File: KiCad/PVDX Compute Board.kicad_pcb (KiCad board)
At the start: 2 copper layers, 66.5 x 64 mm, 43 parts, among them IC1 MIC5350-SGYMT-TR, J1 Conn_02x06_Counter_Clockwise, J2 USB_C_Receptacle_USB2.0_14P, J3 Conn_01x07, J4 Conn_01x06, U1 EM008LX, U2 EM008LX, U3 EM008LX, U4 SAMD51, X1 2x5 0.05" SWD

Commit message: update draft to 11/13 version
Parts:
- added C5: 0.1 uF, Capacitor_SMD:C_0201_0603Metric, F.Cu at (148.3, 54.5)
- added C6: 0.1 uF, Capacitor_SMD:C_0201_0603Metric, F.Cu at (152.8, 54.5)
- added C7: 0.1 uF, Capacitor_SMD:C_0201_0603Metric, F.Cu at (148.3, 75.0)
- added C8: 0.1 uF, Capacitor_SMD:C_0201_0603Metric, F.Cu at (154.8, 75.0)
- added J6: Conn_02x11_Counter_Clockwise, Connector_Hirose:Hirose_DF11-22DP-2DSA_2x11_P2.00mm_Vertical, F.Cu at (173.0, 93.0)
- added R14: 10K, Resistor_SMD:R_0603_1608Metric, F.Cu at (202.0, 72.5)
- added R15: 10K, Resistor_SMD:R_0603_1608Metric, F.Cu at (203.0, 65.3)
- added R16: 10K, Resistor_SMD:R_0603_1608Metric, F.Cu at (151.8, 63.0)
- added R17: 10K, Resistor_SMD:R_0603_1608Metric, F.Cu at (151.7, 74.5)
- added U5: TXS0108EPW, Package_SO:TSSOP-20_4.4x6.5mm_P0.65mm, F.Cu at (151.5, 58.5)
- added U6: TXS0108EPW, Package_SO:TSSOP-20_4.4x6.5mm_P0.65mm, F.Cu at (151.5, 70.0)
- added U7: TMUX1108PW, Package_SO:TSSOP-16_4.4x5mm_P0.65mm, F.Cu at (205.1, 92.0)
- CIN1, CIN4: value 10 μF -> 10 uF
- CIN2: value 0.1 μF -> 0.1 uF
- J3: footprint Connector_Harwin:Harwin_M20-89007xx_1x07_P2.54mm_Horizontal -> Connector_Molex:Molex_Micro-Latch_53253-0770_1x07_P2.00mm_Vertical
- J4: footprint Connector_Harwin:Harwin_M20-89006xx_1x06_P2.54mm_Horizontal -> Connector_Molex:Molex_Micro-Latch_53253-0670_1x06_P2.00mm_Vertical
- L1: value 10 μH -> 10 uH
- R11: footprint Adafruit Grand Central M4 Express rev B:0603-NO -> Resistor_SMD:R_0603_1608Metric
- moved CIN1 61.9 mm to (216.8, 58.5)
- moved CIN2 61.9 mm to (216.8, 60.3)
- moved J1 61.9 mm to (213.8, 59.1)
- moved R7 61.9 mm to (213.4, 68.8)
- moved H3 22.5 mm to (216.1, 96.6)
- moved H4 17.0 mm to (144.4, 96.5)
- moved J4 14.8 mm to (185.3, 25.2)
- moved H2 14.7 mm to (216.1, 24.9)
- moved R3 10.7 mm to (158.0, 48.0), turned to 0 degrees
- moved ON1 8.12 mm to (166.0, 33.5)
- moved R8 7.55 mm to (166.0, 29.5), turned to -90 degrees
- moved J3 7.28 mm to (152.9, 44.0), turned to 90 degrees
- moved H1 2.36 mm to (144.4, 24.9)
- moved R2 2.00 mm to (165.5, 63.0)
- moved R5 0.83 mm to (170.5, 57.0), turned to 90 degrees
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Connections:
- net 3.3V renamed 3V3
- C4 pad 1: 1.8V -> 1V8
- IC1 pad 7: 1.8V -> 1V8
- R1 pad 1: 1.8V -> 1V8
- R1 pad 2: PC14 -> PC14 1V8
- R2 pad 1: 1.8V -> 1V8
- R2 pad 2: PC15 -> PC15 1V8
- R3 pad 1: 1.8V -> 1V8
- R3 pad 2: PC12 -> PC12 1V8
- R4 pad 1: 1.8V -> PC05 1V8
- R4 pad 2: PC05 -> 1V8
- R5 pad 1: 1.8V -> PC07 1V8
- R5 pad 2: PC07 -> 1V8
- R6 pad 1: 1.8V -> PC10 1V8
- R6 pad 2: PC10 -> 1V8
- U1 pad 1: PC04 -> PC04 1V8
- U1 pad 2: PD11 (MISO) -> PD11 (MISO) 1V8
- U1 pad 3: PC14 -> PC14 1V8
- U1 pad 5: PD08 (MOSI) -> PD08 (MOSI) 1V8
- U1 pad 6: PD09 (SCK) -> PD09 (SCK) 1V8
- U1 pad 7: PC05 -> PC05 1V8
- U1 pad 8: 1.8V -> 1V8
- U2 pad 1: PC06 -> PC06 1V8
- U2 pad 2: PD11 (MISO) -> PD11 (MISO) 1V8
- U2 pad 3: PC15 -> PC15 1V8
- U2 pad 5: PD08 (MOSI) -> PD08 (MOSI) 1V8
- U2 pad 6: PD09 (SCK) -> PD09 (SCK) 1V8
- U2 pad 7: PC07 -> PC07 1V8
- U2 pad 8: 1.8V -> 1V8
- U3 pad 1: PC11 -> PC11 1V8
- U3 pad 2: PD11 (MISO) -> PD11 (MISO) 1V8
- U3 pad 3: PC12 -> PC12 1V8
- U3 pad 5: PD08 (MOSI) -> PD08 (MOSI) 1V8
- U3 pad 6: PD09 (SCK) -> PD09 (SCK) 1V8
- U3 pad 7: PC10 -> PC10 1V8
- U3 pad 8: 1.8V -> 1V8
- U4 pad 10: unconnected-(U4B-PA03/AIN01-Pad10) -> AIN01
- U4 pad 125: unconnected-(U4C-PB00/AIN12-Pad125) -> AIN12
- U4 pad 126: unconnected-(U4C-PB01/AIN13-Pad126) -> AIN13
- U4 pad 127: unconnected-(U4C-PB02/AIN14-Pad127) -> AIN14
- U4 pad 128: unconnected-(U4C-PB03/AIN15-Pad128) -> AIN15
- U4 pad 19: unconnected-(U4C-PB08/AIN02-Pad19) -> AIN02
- U4 pad 20: unconnected-(U4C-PB09/AIN03-Pad20) -> AIN03
- U4 pad 21: unconnected-(U4B-PA04/AIN04-Pad21) -> AIN04
- U4 pad 22: unconnected-(U4B-PA05/AIN05-Pad22) -> AIN05
- U4 pad 23: unconnected-(U4B-PA06/AIN06-Pad23) -> AIN06
- U4 pad 24: unconnected-(U4B-PA07/AIN07-Pad24) -> AIN07
- U4 pad 33: unconnected-(U4B-PA08/AIN08-Pad33) -> AIN08
- U4 pad 34: unconnected-(U4B-PA09/AIN09-Pad34) -> AIN09
- U4 pad 35: unconnected-(U4B-PA10/AIN10-Pad35) -> AIN10
- U4 pad 36: unconnected-(U4B-PA11/AIN11-Pad36) -> AIN11
- U4 pad 9: unconnected-(U4B-PA02/AIN00-Pad9) -> AIN00
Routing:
- net 1V8: track 0.00 -> 118.9 mm, vias 0 -> 6
- net 5V: track 48.3 -> 123.1 mm, vias 3 -> 6
- net 1.8V: track 71.7 -> 0.00 mm, vias 2 -> 0
- net GND: track 300.0 -> 370.9 mm, vias 30 -> 25
- net PD21: track 82.2 -> 15.8 mm
- net PD09 (SCK) 1V8: track 0.00 -> 56.8 mm, vias 0 -> 4
- net PC05 1V8: track 0.00 -> 56.5 mm, vias 0 -> 2
- net PD08 (MOSI) 1V8: track 0.00 -> 55.4 mm, vias 0 -> 5
- net PA16 (SCL): track 63.4 -> 17.3 mm, vias 2 -> 0
- net PD11 (MISO) 1V8: track 0.00 -> 44.6 mm, vias 0 -> 5
- net PA17 (SDA): track 62.8 -> 20.6 mm, vias 2 -> 0
- net AIN00: track 0.00 -> 40.5 mm
- net PC05: track 16.9 -> 52.5 mm, vias 2 -> 0
- net PC12 1V8: track 0.00 -> 35.1 mm, vias 0 -> 2
- net PC10 1V8: track 0.00 -> 31.2 mm, vias 0 -> 2
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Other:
- board size 66.5 x 64 mm -> 82.5 x 82.5 mm
- board text added: "3V3"
- board text added: "5V"
- board text added: "ARDUCAM"
- board text added: "CS"
- board text added: "DRDY"
- board text added: "GND"
- board text added: "MAGNETOMETER"
- board text added: "MISO"
- board text added: "MOSI"
- board text added: "OLED"
- board text added: "P01A"
- board text added: "P01B"
- board text added: "P02A"
- board text added: "P02B"
- board text added: "P03A"
- board text added: "P03B"
- board text added: "P04A"
- board text added: "P04B"
- board text added: "P05A"
- board text added: "P05B"
- board text added: "P06A"
- board text added: "P06B"
- board text added: "P07A"
- board text added: "P07B"
- board text added: "P08A"
- board text added: "P08B"
- board text added: "P09A"
- board text added: "P09B"
- board text added: "P10A"
- board text added: "P10B"
- board text added: "P11A"
- board text added: "P11B"
- board text added: "PHOTODIODES"
- board text added: "REXT"
- board text added: "SCK"
- board text added: "SCL"
- board text added: "SDA"
- board text added: "~{CS}"
- board text added: "~{D/C}"
- board text added: "~{RES}"
- board text removed: "PVDX COMPUTE BOARD FLATSAT V1 2025-04-06"

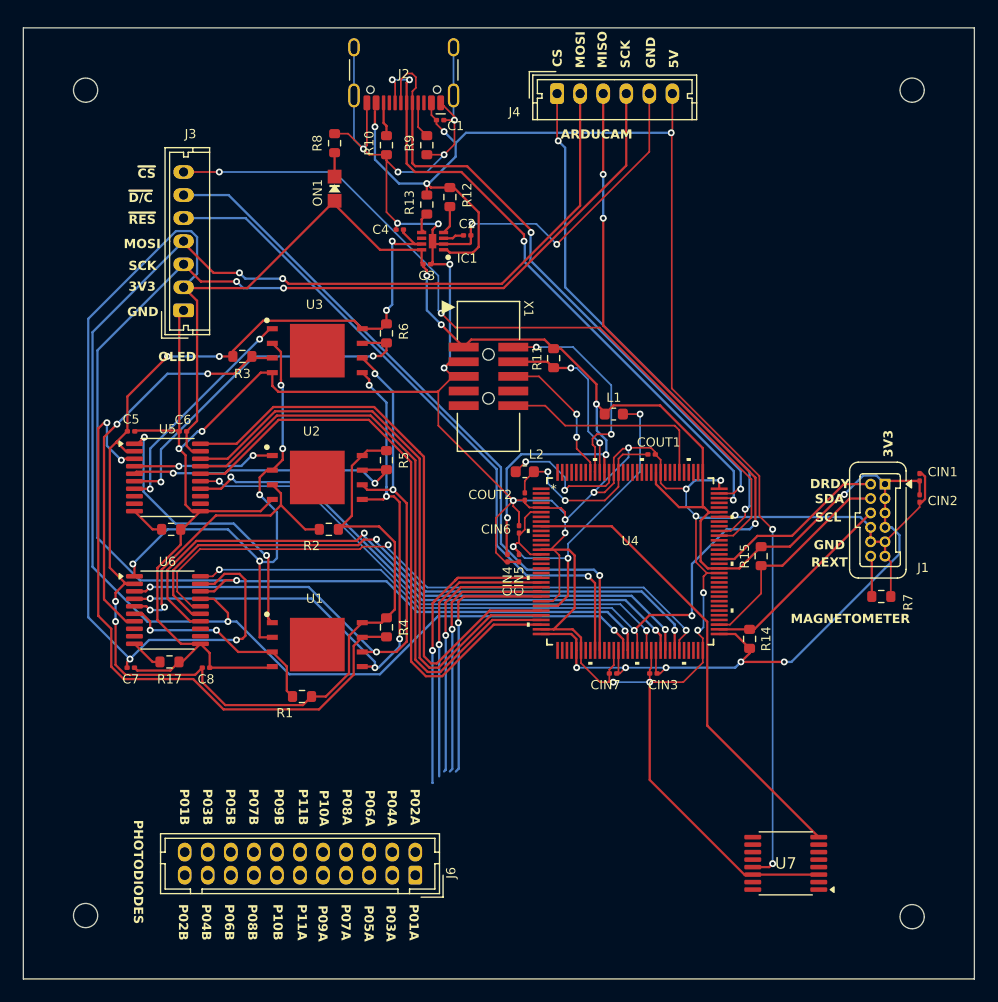
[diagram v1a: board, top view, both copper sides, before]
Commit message: Redid layout to separate analog/digital traces
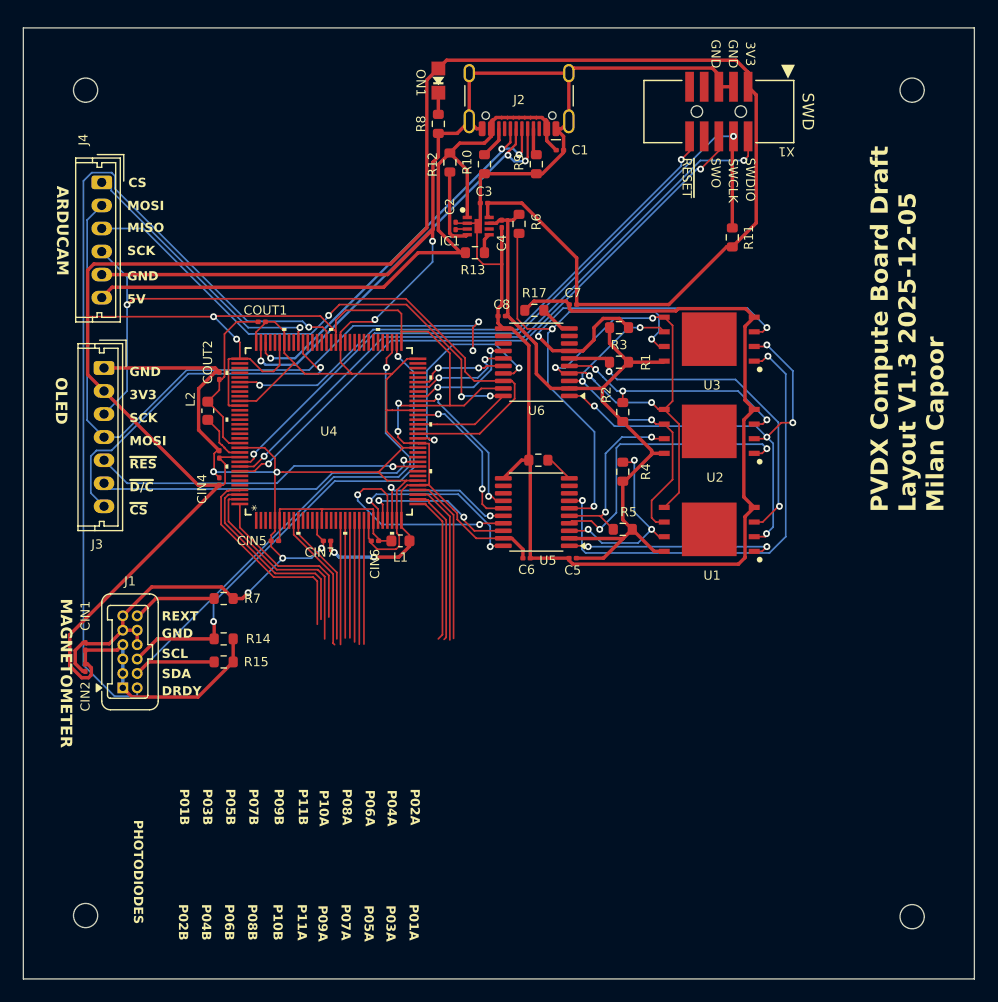
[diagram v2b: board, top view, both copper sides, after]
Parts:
- removed J6: Conn_02x11_Counter_Clockwise, Connector_Hirose:Hirose_DF11-22DP-2DSA_2x11_P2.00mm_Vertical
- removed U7: TMUX1108PW, Package_SO:TSSOP-16_4.4x5mm_P0.65mm
- moved CIN1 73.8 mm to (144.4, 73.2)
- moved CIN2 73.8 mm to (144.4, 75.0)
- moved J1 68.4 mm to (147.6, 76.8), turned to 90 degrees
- moved R7 57.0 mm to (156.4, 69.0)
- moved C7 49.6 mm to (186.7, 43.5), turned to 180 degrees
- moved R15 47.5 mm to (156.4, 74.5), turned to 0 degrees
- moved R14 45.6 mm to (156.4, 72.5), turned to 0 degrees
- moved R17 44.0 mm to (183.3, 44.0), turned to 180 degrees
- moved CIN3 42.2 mm to (156.0, 56.5), turned to 90 degrees
- moved J4 40.2 mm to (145.8, 32.9), turned to -90 degrees
- moved R1 40.0 mm to (190.7, 48.5)
- moved C5 39.9 mm to (186.7, 65.5), turned to 180 degrees
- moved C8 39.9 mm to (180.5, 44.5), turned to 180 degrees
- moved U6 38.6 mm to (183.5, 48.5), turned to 180 degrees
- moved COUT1 35.7 mm to (159.7, 45.0)
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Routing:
- net PD09 (SCK): track 131.2 -> 64.4 mm, vias 4 -> 1
- net PD21: track 15.8 -> 77.3 mm, vias 0 -> 1
- net 5V: track 123.1 -> 62.8 mm, vias 6 -> 0
- net PD08 (MOSI): track 137.7 -> 80.5 mm
- net 1V8: track 118.9 -> 64.6 mm, vias 6 -> 0
- net PD11 (MISO): track 101.8 -> 53.4 mm, vias 6 -> 3
- net SWCLK: track 15.6 -> 62.7 mm
- net PC15: track 54.7 -> 8.24 mm
- net PC14: track 55.3 -> 9.18 mm
- net PC12: track 56.1 -> 10.2 mm
- net SWO: track 12.4 -> 54.4 mm
- net PC05 1V8: track 56.5 -> 17.2 mm, vias 2 -> 3
- net PC07: track 52.7 -> 13.6 mm, vias 0 -> 2
- net PC05: track 52.5 -> 13.9 mm, vias 0 -> 2
- net SWDIO: track 19.0 -> 57.0 mm
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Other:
- board text added: "PVDX Compute Board Draft Layout V1.3 2025-12-05 Milan Capoor"
- board text added: "SWCLK"
- board text added: "SWD"
- board text added: "SWDIO"
- board text added: "SWO"
- board text added: "~{RESET}"
- board text removed: "CIN3"

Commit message: updated pins to match new spec and exposed all pins
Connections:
- U4 pad 11: unconnected-(U4C-PB04-Pad11) -> AIN06
- U4 pad 12: unconnected-(U4C-PB05-Pad12) -> AIN07
- U4 pad 127: AIN14 -> unconnected-(U4C-PB02/AIN14-Pad127)
- U4 pad 128: AIN15 -> unconnected-(U4C-PB03/AIN15-Pad128)
- U4 pad 13: unconnected-(U4E-PD00-Pad13) -> AIN14
- U4 pad 16: unconnected-(U4E-PD01-Pad16) -> AIN15
- U4 pad 17: unconnected-(U4C-PB06-Pad17) -> AIN08
- U4 pad 18: unconnected-(U4C-PB07-Pad18) -> AIN09
- U4 pad 21: AIN04 -> unconnected-(U4B-PA04/AIN04-Pad21)
- U4 pad 22: AIN05 -> unconnected-(U4B-PA05/AIN05-Pad22)
- U4 pad 23: AIN06 -> unconnected-(U4B-PA06/AIN06-Pad23)
- U4 pad 24: AIN07 -> unconnected-(U4B-PA07/AIN07-Pad24)
- U4 pad 3: unconnected-(U4D-PC00-Pad3) -> AIN10
- U4 pad 33: AIN08 -> unconnected-(U4B-PA08/AIN08-Pad33)
- U4 pad 34: AIN09 -> unconnected-(U4B-PA09/AIN09-Pad34)
- U4 pad 35: AIN10 -> unconnected-(U4B-PA10/AIN10-Pad35)
- U4 pad 36: AIN11 -> unconnected-(U4B-PA11/AIN11-Pad36)
- U4 pad 4: unconnected-(U4D-PC01-Pad4) -> AIN11
- U4 pad 7: unconnected-(U4D-PC02-Pad7) -> AIN04
- U4 pad 8: unconnected-(U4D-PC03-Pad8) -> AIN05
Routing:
- net unconnected-(U4C-PB02/AIN14-Pad127): track 0.00 -> 18.6 mm
- net AIN14: track 18.6 -> 0.00 mm
- net unconnected-(U4C-PB03/AIN15-Pad128): track 0.00 -> 15.1 mm
- net AIN15: track 15.1 -> 0.00 mm
- net unconnected-(U4B-PA11/AIN11-Pad36): track 0.00 -> 14.7 mm
- net AIN11: track 14.7 -> 0.00 mm
- net unconnected-(U4B-PA10/AIN10-Pad35): track 0.00 -> 14.3 mm
- net AIN10: track 14.3 -> 0.00 mm
- net unconnected-(U4B-PA09/AIN09-Pad34): track 0.00 -> 13.8 mm
- net AIN09: track 13.8 -> 0.00 mm
- net unconnected-(U4B-PA08/AIN08-Pad33): track 0.00 -> 13.1 mm
- net AIN08: track 13.1 -> 0.00 mm
- net unconnected-(U4B-PA06/AIN06-Pad23): track 0.00 -> 10.7 mm
- net AIN06: track 10.7 -> 0.00 mm
- net unconnected-(U4B-PA07/AIN07-Pad24): track 0.00 -> 10.7 mm
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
